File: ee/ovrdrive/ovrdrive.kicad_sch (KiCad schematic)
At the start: 42 parts, among them J1 USB_A, J2 Conn_01x02_Female, J3 AVR-ISP-6, Q1 Q_NMOS_DGS, U1 SM3257ENT, U2 FLASH, U3 ATtiny24A-MM, U4 74AUC1G32, U5 LMV321, U6 LM4040DBZ-2.5

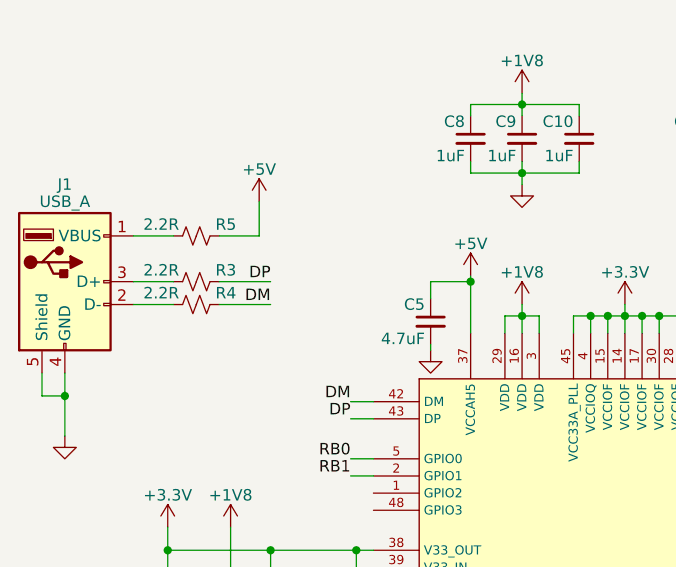
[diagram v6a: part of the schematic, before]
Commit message: Routed out the power.
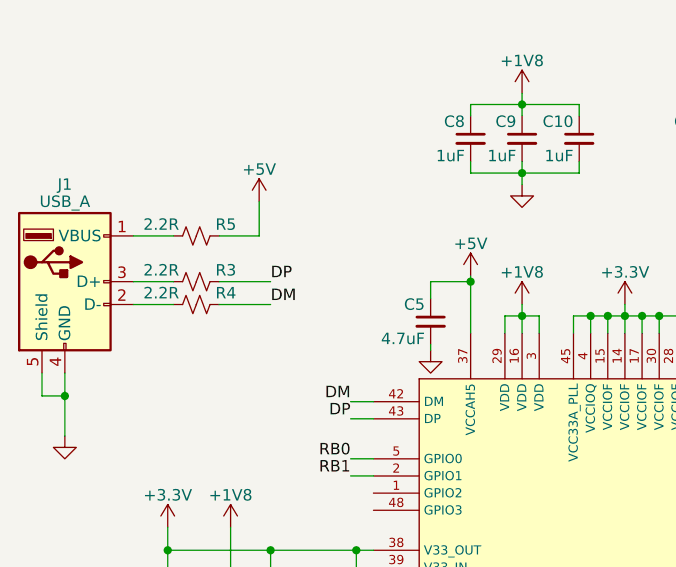
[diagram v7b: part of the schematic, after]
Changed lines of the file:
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@@
     (effects (font (size 1 1)) (justify left bottom))
   )
-  (label "DP" (at 43.18 59.055 180)
-    (effects (font (size 1.27 1.27)) (justify right bottom))
+  (label "DP" (at 43.18 59.055 0)
+    (effects (font (size 1.27 1.27)) (justify left bottom))
   )
   (label "RB0" (at 52.07 78.74 180)
@@
     (effects (font (size 1 1)) (justify left bottom))
   )
-  (label "DM" (at 43.18 61.595 180)
-    (effects (font (size 1.27 1.27)) (justify right bottom))
+  (label "DM" (at 43.18 61.595 0)
+    (effects (font (size 1.27 1.27)) (justify left bottom))
   )
   (label "~{RE}" (at 173.355 100.965 0)

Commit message: Working on the routing.
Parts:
- added C15: 100nF, Capacitor_SMD:C_0603_1608Metric, symbol Device:C_Small
- U2: footprint SOP50P2000X120-48N -> TSOP48:tsop48
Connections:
- net +5V: now also C15.1
- net GND: now also C15.2
- net FD7: now reaches U1.10 (FD7), U2.44 (I/O7)
- net FD6: now reaches U1.11 (FD6), U2.43 (I/O6)
- net FD5: now reaches U1.12 (FD5), U2.42 (I/O5)
- net FD4: now reaches U1.13 (FD4), U2.41 (I/O4)
- net FD3: now reaches U1.18 (FD3), U2.32 (I/O3)
- net FD2: now reaches U1.19 (FD2), U2.31 (I/O2)
- net FD1: now reaches U1.20 (FD1), U2.30 (I/O1)
- net FD0: now reaches U1.21 (FD0), U2.29 (I/O0)
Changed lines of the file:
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@@
   (junction (at 74.93 125.095) (diameter 0) (color 0 0 0 0)
   )
+  (junction (at 236.22 140.335) (diameter 0) (color 0 0 0 0)
+  )
   (junction (at 38.735 92.71) (diameter 0) (color 0 0 0 0)
   )
@@
     (stroke (width 0) (type default) (color 0 0 0 0))
   )
+  (wire (pts (xy 236.22 140.335) (xy 236.22 141.605))
+    (stroke (width 0) (type default) (color 0 0 0 0))
+  )
   (wire (pts (xy 52.705 154.305) (xy 48.26 154.305))
     (stroke (width 0) (type default) (color 0 0 0 0))
@@
   )
   (wire (pts (xy 84.455 62.865) (xy 82.55 62.865))
+    (stroke (width 0) (type default) (color 0 0 0 0))
+  )
+  (wire (pts (xy 236.22 146.685) (xy 236.22 148.59))
     (stroke (width 0) (type default) (color 0 0 0 0))
   )
@@
     (effects (font (size 1.27 1.27)) (justify right bottom))
   )
+  (label "FD0" (at 104.775 93.345 0)
+    (effects (font (size 1.27 1.27)) (justify left bottom))
+  )
+  (label "FD5" (at 104.775 102.87 0)
+    (effects (font (size 1.27 1.27)) (justify left bottom))
+  )
   (label "RB0" (at 137.16 87.63 180)
     (effects (font (size 1.27 1.27)) (justify right bottom))
   )
+  (label "FD7" (at 104.775 106.68 0)
+    (effects (font (size 1.27 1.27)) (justify left bottom))
+  )
   (label "SCK" (at 101.6 153.035 180)
     (effects (font (size 1.27 1.27)) (justify right bottom))
   )
+  (label "FD6" (at 104.775 104.775 0)
+    (effects (font (size 1.27 1.27)) (justify left bottom))
+  )
   (label "DQS" (at 173.355 106.68 0)
     (effects (font (size 1 1)) (justify left bottom))
@@
     (effects (font (size 1.27 1.27)) (justify right bottom))
   )
+  (label "FD2" (at 104.775 97.155 0)
+    (effects (font (size 1.27 1.27)) (justify left bottom))
+  )
   (label "INHIBIT" (at 86.995 157.48 0)
     (effects (font (size 1 1)) (justify left bottom))
@@
     (effects (font (size 1 1)) (justify right bottom))
   )
+  (label "FD1" (at 104.775 95.25 0)
+    (effects (font (size 1.27 1.27)) (justify left bottom))
+  )
   (label "~{CE2}" (at 104.775 87.63 0)
     (effects (font (size 1 1)) (justify left bottom))
@@
     (effects (font (size 1.27 1.27)) (justify right bottom))
   )
+  (label "FD4" (at 104.775 100.965 0)
+    (effects (font (size 1.27 1.27)) (justify left bottom))
+  )
   (label "~{CE2}" (at 175.895 94.615 0)
     (effects (font (size 1 1)) (justify left bottom))
@@
   (label "ALE" (at 173.355 87.63 0)
     (effects (font (size 1 1)) (justify left bottom))
+  )
+  (label "FD3" (at 104.775 99.06 0)
+    (effects (font (size 1.27 1.27)) (justify left bottom))
   )
   (label "~{WE}" (at 173.355 102.87 0)
@@
     (property "Reference" "U2" (id 0) (at 264.16 16.671 0))
     (property "Value" "FLASH" (id 1) (at 264.16 19.2079 0))
-    (property "Footprint" "SOP50P2000X120-48N" (id 2) (at 263.525 29.21 0)
+    (property "Footprint" "TSOP48:tsop48" (id 2) (at 263.525 29.21 0)
       (effects (font (size 1.27 1.27)) (justify left bottom) hide)
     )
@@
     (pin "1")
   )
+  (symbol (lib_id "power:GND") (at 236.22 148.59 0) (mirror y) (unit 1)
+    (in_bom yes) (on_board yes) (fields_autoplaced)
+    (property "Reference" "#PWR0107" (id 0) (at 236.22 154.94 0)
+      (effects (font (size 1.27 1.27)) hide)
+    )
+    (property "Value" "GND" (id 1) (at 236.22 153.0334 0)
+      (effects (font (size 1.27 1.27)) hide)
+    )
+    (property "Footprint" "" (id 2) (at 236.22 148.59 0)
+      (effects (font (size 1.27 1.27)) hide)
+    )
+    (property "Datasheet" "" (id 3) (at 236.22 148.59 0)
+      (effects (font (size 1.27 1.27)) hide)
+    )
+    (pin "1")
+  )
   (symbol (lib_id "Device:C_Small") (at 149.225 72.39 0) (unit 1)
     (in_bom yes) (on_board yes)
@@
     (pin "2")
   )
+  (symbol (lib_id "Device:C_Small") (at 236.22 144.145 0) (unit 1)
+    (in_bom yes) (on_board yes)
+    (property "Reference" "C15" (id 0) (at 234.95 142.24 0)
+      (effects (font (size 1.27 1.27)) (justify right))
+    )
+    (property "Value" "100nF" (id 1) (at 235.585 146.05 0)
+      (effects (font (size 1.27 1.27)) (justify right))
+    )
+    (property "Footprint" "Capacitor_SMD:C_0603_1608Metric" (id 2) (at 236.22 144.145 0)
+      (effects (font (size 1.27 1.27)) hide)
+    )
+    (property "Datasheet" "~" (id 3) (at 236.22 144.145 0)
+      (effects (font (size 1.27 1.27)) hide)
+    )
+    (pin "1")
+    (pin "2")
+  )
   (symbol (lib_id "power:GND") (at 149.225 77.47 0) (unit 1)
     (in_bom yes) (on_board yes)
@@
       (effects (font (size 1.27 1.27)) (justify right))
     )
-    (property "Footprint" "SOP50P2000X120-48N" (id 2) (at 155.575 83.82 0)
+    (property "Footprint" "TSOP48:tsop48" (id 2) (at 155.575 83.82 0)
       (effects (font (size 1.27 1.27)) (justify left bottom) hide)
     )
@@
       (reference "#PWR0106") (unit 1) (value "GND") (footprint "")
     )
+    (path "/2e0e710a-416e-4386-8871-f0cb2d45cee1"
+      (reference "#PWR0107") (unit 1) (value "GND") (footprint "")
+    )
     (path "/d60b468a-6439-461a-a0cb-6f3bf93d3fdd"
       (reference "C1") (unit 1) (value "100nF") (footprint "Capacitor_SMD:C_0603_1608Metric")
@@
       (reference "C14") (unit 1) (value "100nF") (footprint "Capacitor_SMD:C_0603_1608Metric")
     )
+    (path "/8c0fed10-1c30-421b-a591-e885f8a8dab1"
+      (reference "C15") (unit 1) (value "100nF") (footprint "Capacitor_SMD:C_0603_1608Metric")
+    )
     (path "/22a5d4c1-9fe9-4078-9244-2cd11203f2b1"
       (reference "C17") (unit 1) (value "1uF") (footprint "Capacitor_SMD:C_0603_1608Metric")
@@
     )
     (path "/ef4d2253-714f-451d-bc3d-d57ac3c20e1d"
-      (reference "U2") (unit 1) (value "FLASH") (footprint "SOP50P2000X120-48N")
+      (reference "U2") (unit 1) (value "FLASH") (footprint "TSOP48:tsop48")
     )
     (path "/227ecb9d-f74a-4686-8c23-33378965f459"
-      (reference "U2") (unit 2) (value "FLASH") (footprint "SOP50P2000X120-48N")
+      (reference "U2") (unit 2) (value "FLASH") (footprint "TSOP48:tsop48")
     )
     (path "/493cf60e-8351-428d-a243-907030862903"
